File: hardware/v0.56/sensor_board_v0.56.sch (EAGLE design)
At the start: 65 parts, among them J3 USB-MICROB, U1 NEOPIXEL_NANO_2427, U10 TSL2591, U11 915MHz, U12 MH-Z19, U13 CCS811-I2C, U14 IAQ-CORE-C, U15 VLP-450-F, U16 VLP-450-F, U2 FT231XQ-R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

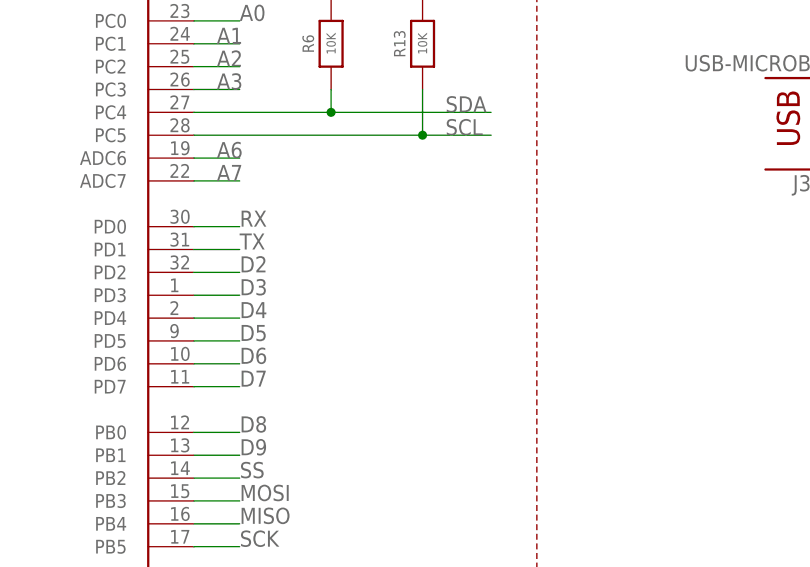
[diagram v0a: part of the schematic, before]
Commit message: Added another decoupling cap to ATMega328P
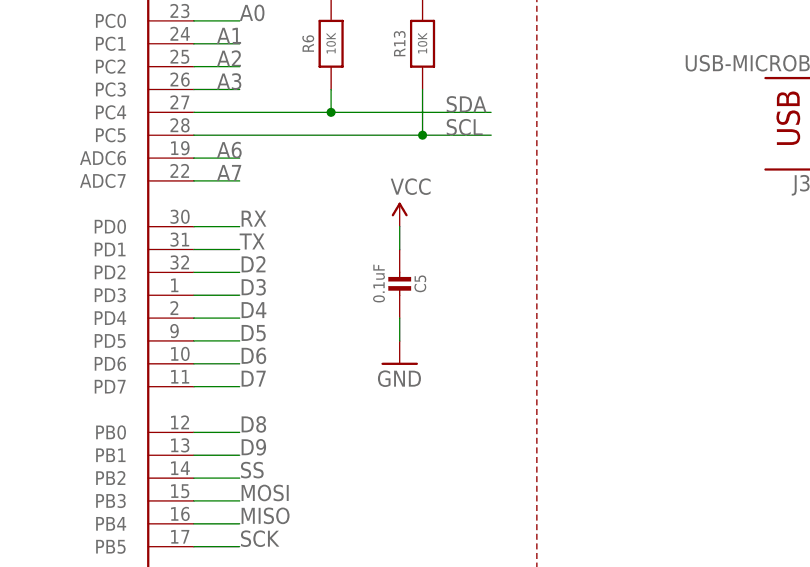
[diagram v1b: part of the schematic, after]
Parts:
- added C5: 0.1uF, Adafruit Feather 32u4 Bluefruit LE:MICROBUILDER_CAP_CERAMIC_0402MP
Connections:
- net GND: now also C5.1
- net VCC: now also C5.2
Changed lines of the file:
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@@
 <part name="U15" library="VLP-450-F" deviceset="VLP-450-F" device=""/>
 <part name="U16" library="VLP-450-F" deviceset="VLP-450-F" device=""/>
+<part name="C5" library="Adafruit Feather 32u4 Bluefruit LE" deviceset="MICROBUILDER_CAP_CERAMIC" device="_0402MP" value="0.1uF"/>
+<part name="SUPPLY17" library="SparkFun-Aesthetics" deviceset="VCC" device=""/>
+<part name="GND13" library="SparkFun-Aesthetics" deviceset="GND" device=""/>
 </parts>
 <sheets>
@@
 <instance part="U15" gate="G$1" x="226.06" y="-73.66"/>
 <instance part="U16" gate="G$1" x="226.06" y="-83.82"/>
+<instance part="C5" gate="G$1" x="38.1" y="-71.12" rot="R180"/>
+<instance part="SUPPLY17" gate="G$1" x="38.1" y="-66.04"/>
+<instance part="GND13" gate="1" x="38.1" y="-81.28"/>
 </instances>
 <busses>
@@
 <junction x="83.82" y="-5.08"/>
 </segment>
+<segment>
+<pinref part="GND13" gate="1" pin="GND"/>
+<pinref part="C5" gate="G$1" pin="1"/>
+<wire x1="38.1" y1="-78.74" x2="38.1" y2="-76.2" width="0.1524" layer="91"/>
+</segment>
 </net>
 <net name="VCC" class="0">
@@
 <pinref part="SUPPLY5" gate="G$1" pin="VCC"/>
 </segment>
+<segment>
+<pinref part="C5" gate="G$1" pin="2"/>
+<pinref part="SUPPLY17" gate="G$1" pin="VCC"/>
+<wire x1="38.1" y1="-68.58" x2="38.1" y2="-66.04" width="0.1524" layer="91"/>
+</segment>
 </net>

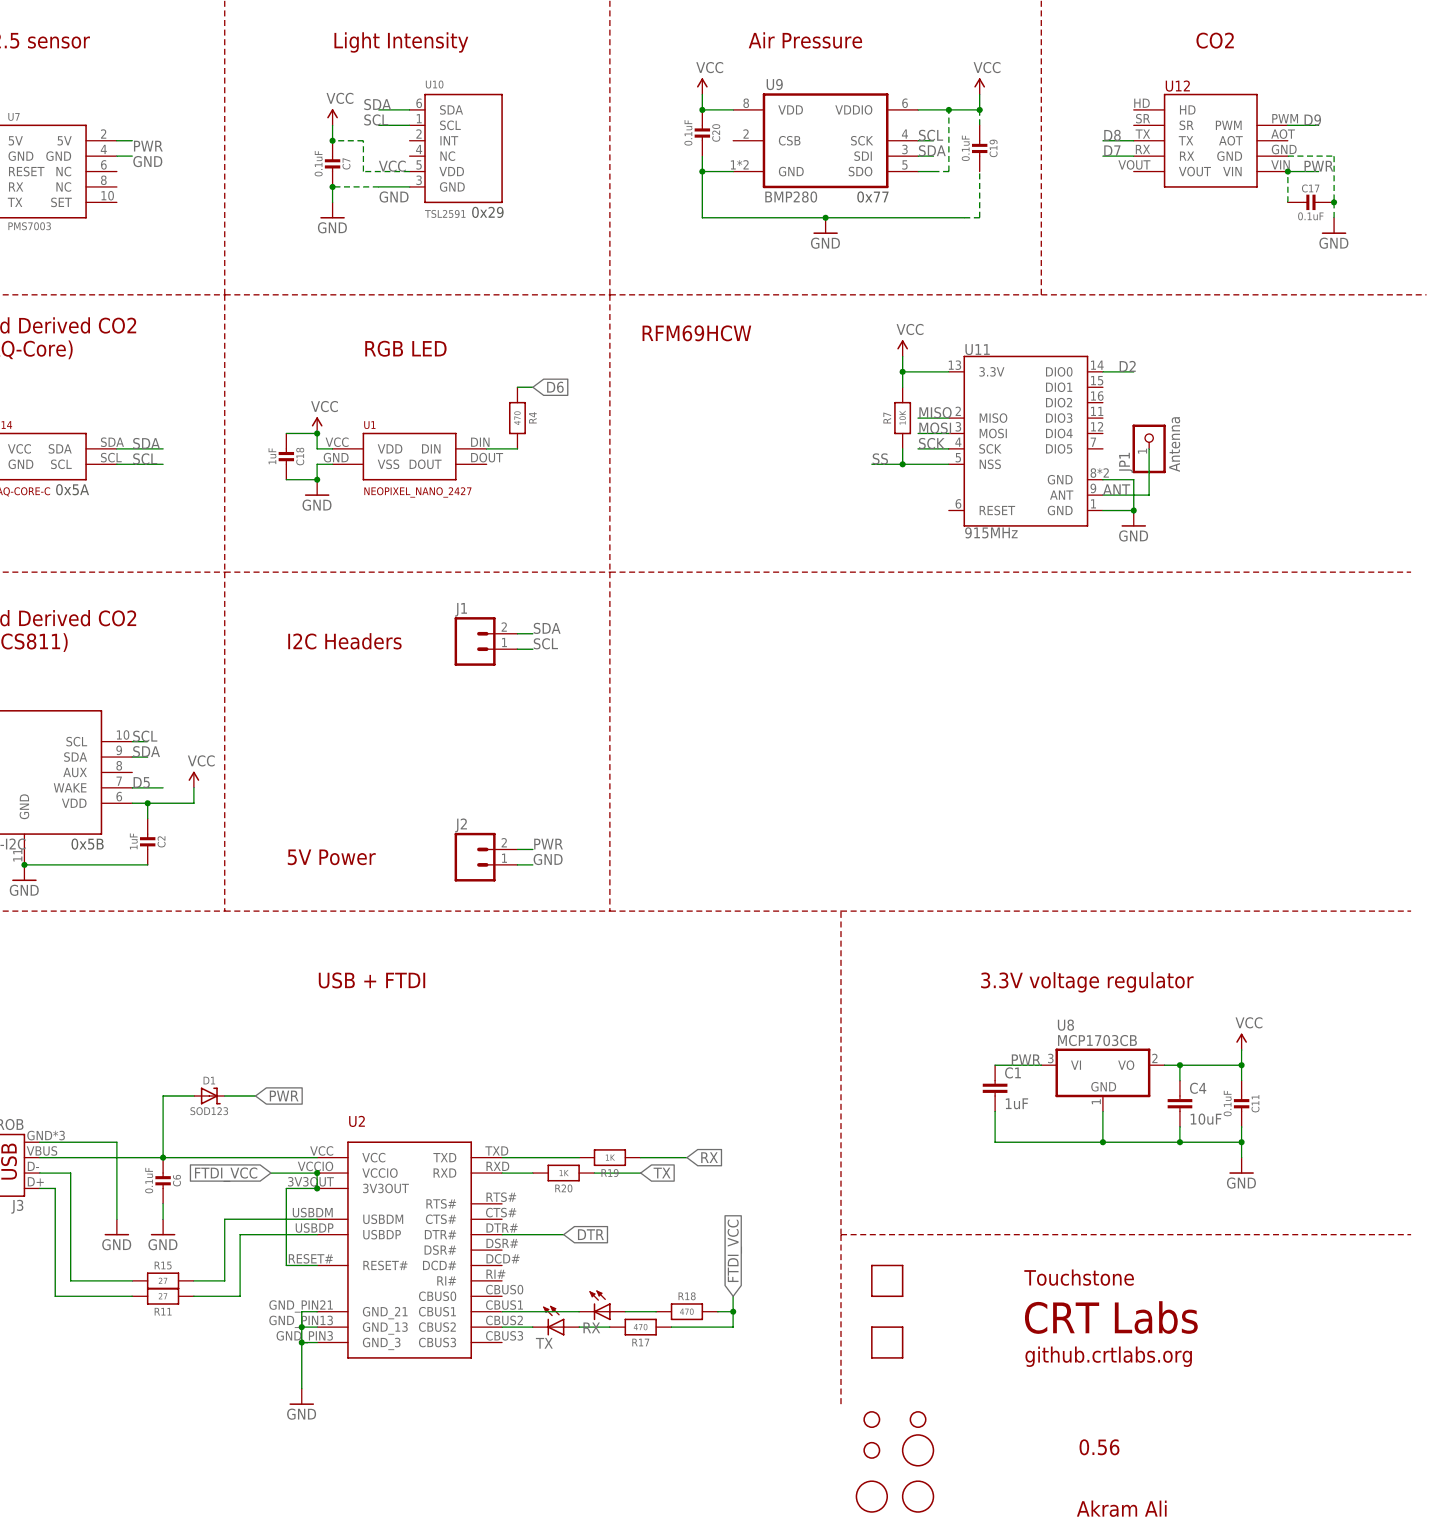
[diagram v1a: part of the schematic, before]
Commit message: v0.56b - minor adjustments
- Rerouted D9 trace to be SET pin for PM sensor instead of PWM pin for
CO2 sensor
- Added 10K pull up on D9
- Moved components away from light sensor and RGB LED's light pipe's
path
- Added extra vias all around for more ground stitching
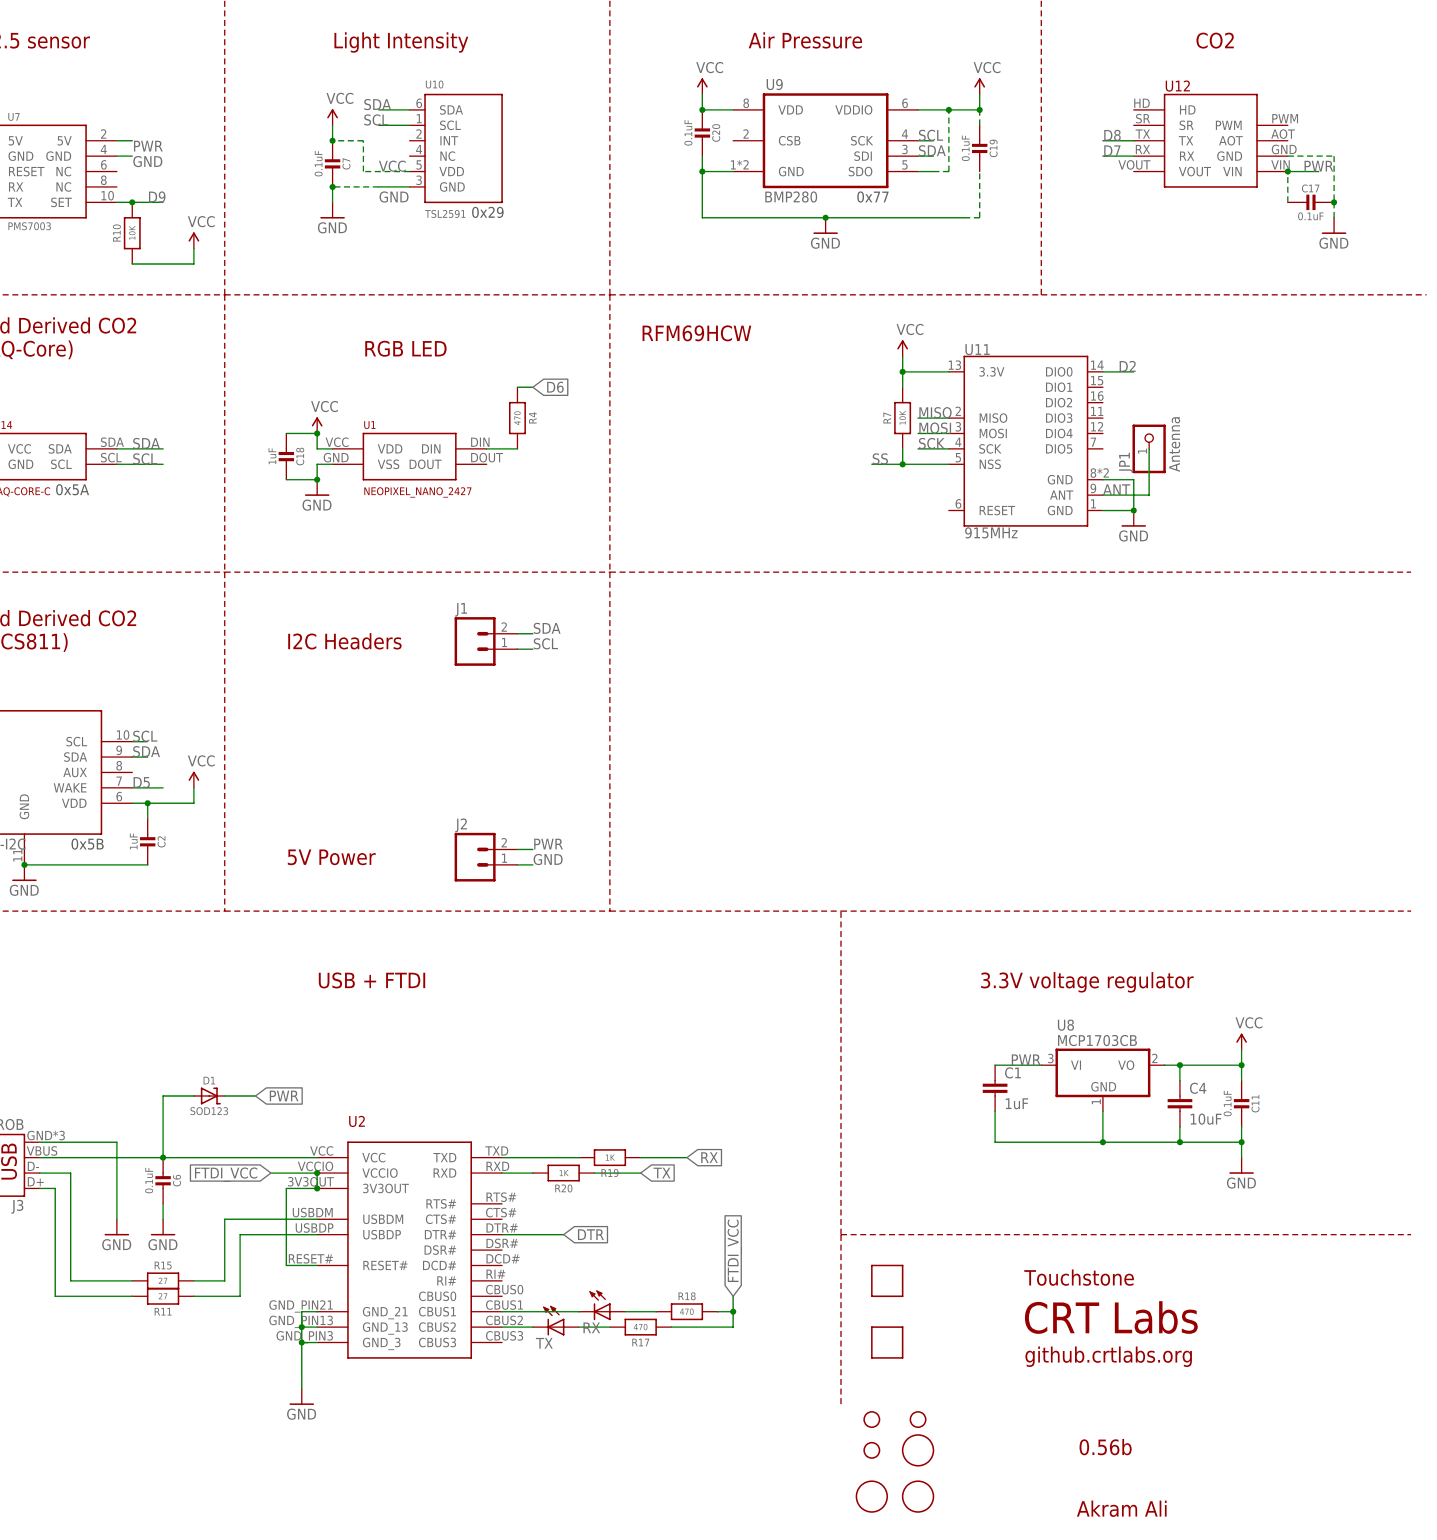
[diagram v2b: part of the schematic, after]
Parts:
- added R10: 10K, Adafruit Feather 32u4 Bluefruit LE:MICROBUILDER_RESISTOR_0402MP
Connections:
- net D9: now also R10.2, U7.SET; no longer U12.PWM
- net VCC: now also R10.1
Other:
- note added: "0.56b"
- note removed: "0.56"
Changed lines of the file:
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@@
 <part name="SUPPLY17" library="SparkFun-Aesthetics" deviceset="VCC" device=""/>
 <part name="GND13" library="SparkFun-Aesthetics" deviceset="GND" device=""/>
+<part name="R10" library="Adafruit Feather 32u4 Bluefruit LE" deviceset="MICROBUILDER_RESISTOR" device="_0402MP" value="10K"/>
+<part name="SUPPLY18" library="SparkFun-Aesthetics" deviceset="VCC" device=""/>
 </parts>
 <sheets>
@@
 <text x="88.9" y="55.88" size="1.778" layer="97">0x5A</text>
 <text x="220.98" y="104.14" size="1.778" layer="97">0x77</text>
-<text x="257.556" y="-102.362" size="2.54" layer="94" font="vector" ratio="10">0.56</text>
+<text x="257.556" y="-102.362" size="2.54" layer="94" font="vector" ratio="10">0.56b</text>
 <text x="248.666" y="-87.122" size="2.54" layer="94" font="vector" ratio="10">github.crtlabs.org</text>
 <text x="157.48" y="101.6" size="1.778" layer="97">0x29</text>
@@
 <instance part="SUPPLY17" gate="G$1" x="38.1" y="-66.04"/>
 <instance part="GND13" gate="1" x="38.1" y="-81.28"/>
+<instance part="R10" gate="G$1" x="101.6" y="99.06" rot="R90"/>
+<instance part="SUPPLY18" gate="G$1" x="111.76" y="96.52"/>
 </instances>
 <busses>
@@
 <wire x1="38.1" y1="-68.58" x2="38.1" y2="-66.04" width="0.1524" layer="91"/>
 </segment>
+<segment>
+<pinref part="R10" gate="G$1" pin="1"/>
+<wire x1="101.6" y1="93.98" x2="111.76" y2="93.98" width="0.1524" layer="91"/>
+<wire x1="111.76" y1="93.98" x2="111.76" y2="96.52" width="0.1524" layer="91"/>
+<pinref part="SUPPLY18" gate="G$1" pin="VCC"/>
+</segment>
 </net>
 <net name="SCL" class="0">
@@
 </segment>
 <segment>
-<pinref part="U12" gate="G$1" pin="PWM"/>
-<wire x1="292.1" y1="116.84" x2="297.18" y2="116.84" width="0.1524" layer="91"/>
-<label x="294.64" y="116.84" size="1.778" layer="95"/>
-</segment>
-</net>
+<pinref part="U7" gate="G$1" pin="SET"/>
+<label x="104.14" y="104.14" size="1.778" layer="95"/>
+<pinref part="R10" gate="G$1" pin="2"/>
+<wire x1="99.06" y1="104.14" x2="101.6" y2="104.14" width="0.1524" layer="91"/>
+<wire x1="101.6" y1="104.14" x2="106.68" y2="104.14" width="0.1524" layer="91"/>
+<junction x="101.6" y="104.14"/>
+</segment>
+</net>
